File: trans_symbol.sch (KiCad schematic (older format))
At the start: 17 parts, among them J4 Conn_01x04, SW1 SW_SPST, U1 ATSAMD21G18A-AU, U2 MIC5504-3.3YM5, Y1 32768Hz

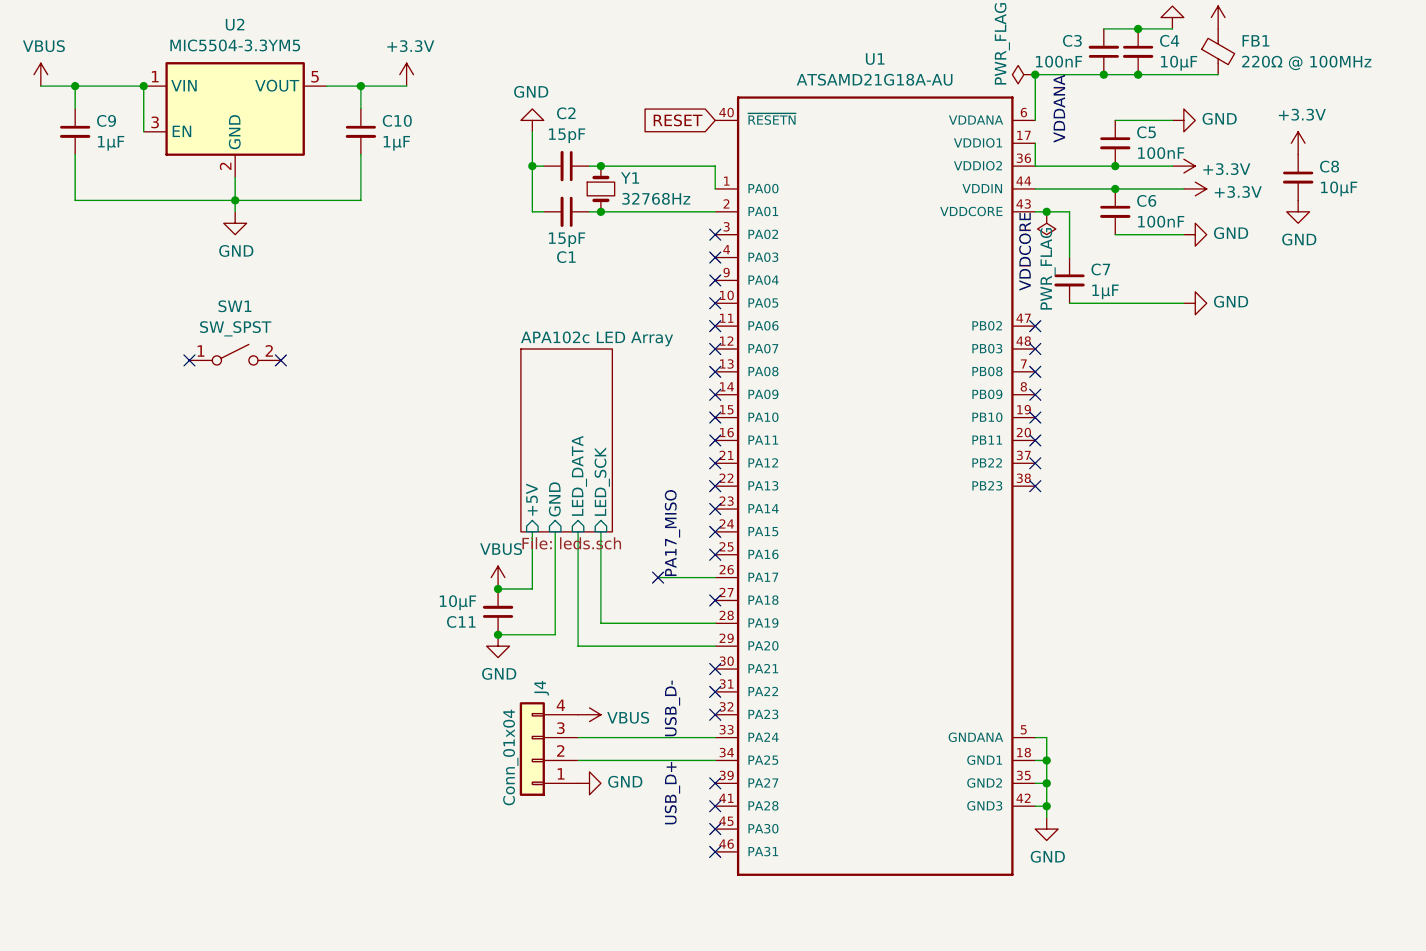
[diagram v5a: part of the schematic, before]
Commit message: add an i2s microphone on default arduino zero i2s pins
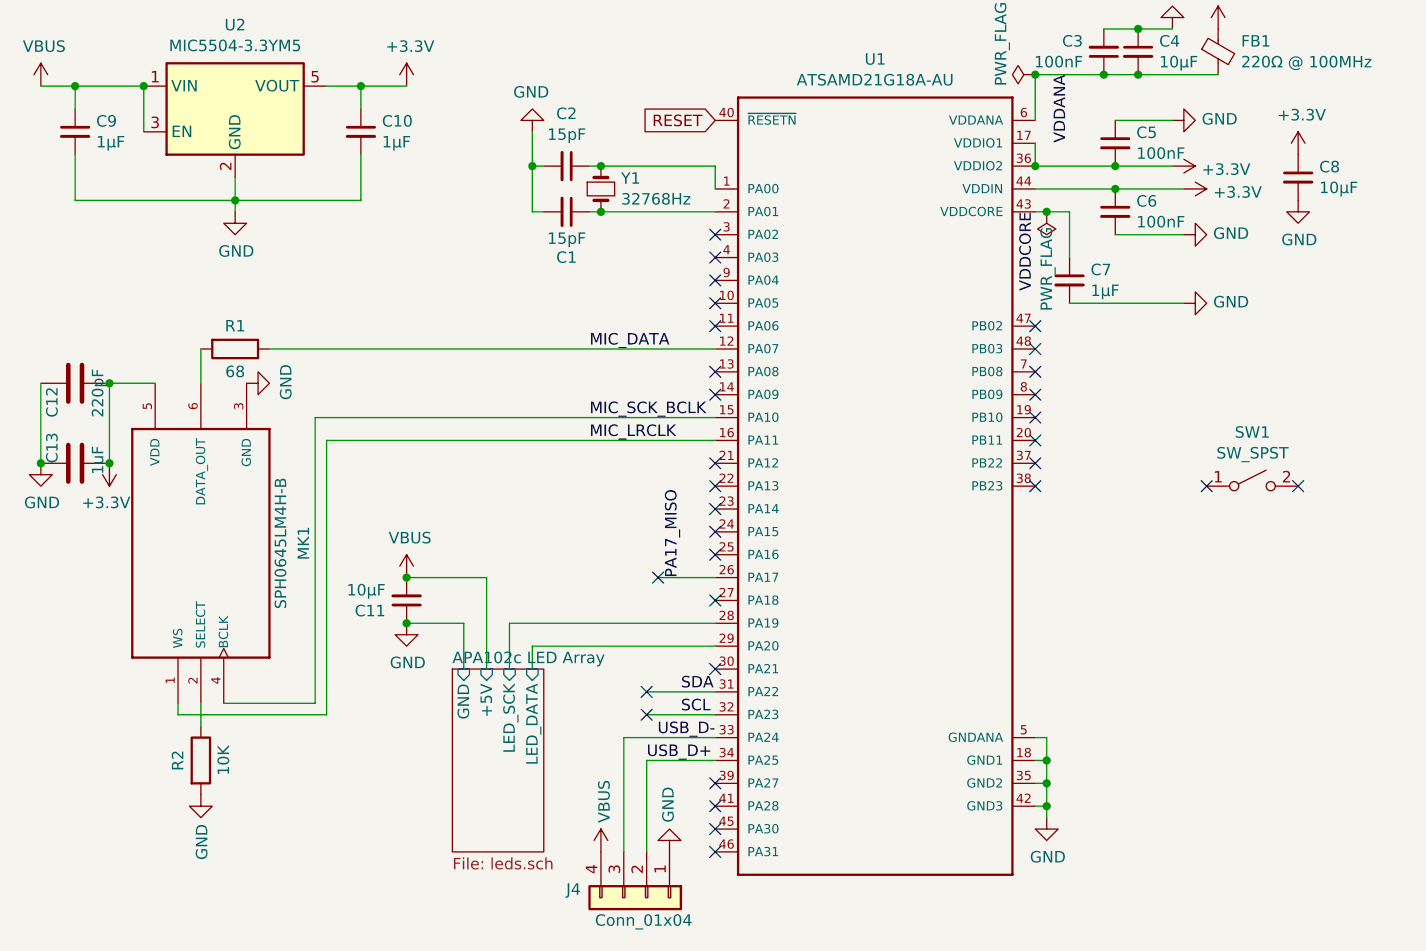
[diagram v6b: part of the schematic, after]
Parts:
- added C12: 220pF, Capacitor_SMD:C_0805_2012Metric, symbol Device:C
- added C13: 1uF, Capacitor_SMD:C_0805_2012Metric, symbol Device:C
- added MK1: SPH0645LM4H-B, Mic-SPH0645LM4H-B:MIC_SPH0645LM4H-B, symbol Mic_I2S_SPH0645LM4H-B:SPH0645LM4H-B
- added R1: 68, Resistor_SMD:R_0805_2012Metric, symbol Device:R
- added R2: 10K, Resistor_SMD:R_0603_1608Metric, symbol Device:R
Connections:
- net +3V3: now also C12.2, C13.2, MK1.5 (VDD)
- net GND: now also C12.1, C13.1, MK1.3 (GND), R2.2
- net MIC_DATA: now reaches U1.12 (PA07)
- net MIC_DATA: now also R1.1
- net MIC_SCK_BCLK: now reaches U1.15 (PA10)
- net MIC_SCK_BCLK: now also MK1.4 (BCLK)
- net MIC_LRCLK: now reaches U1.16 (PA11)
- net MIC_LRCLK: now also MK1.1 (WS)
- net SDA: now reaches U1.31 (PA22)
- net SCL: now reaches U1.32 (PA23)
- new net: MK1.2 (SELECT), R2.1
- new net: MK1.6 (DATA_OUT), R1.2
- no-connect marks 34 -> 31
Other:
- moved on the sheet: C11, J4, SW1

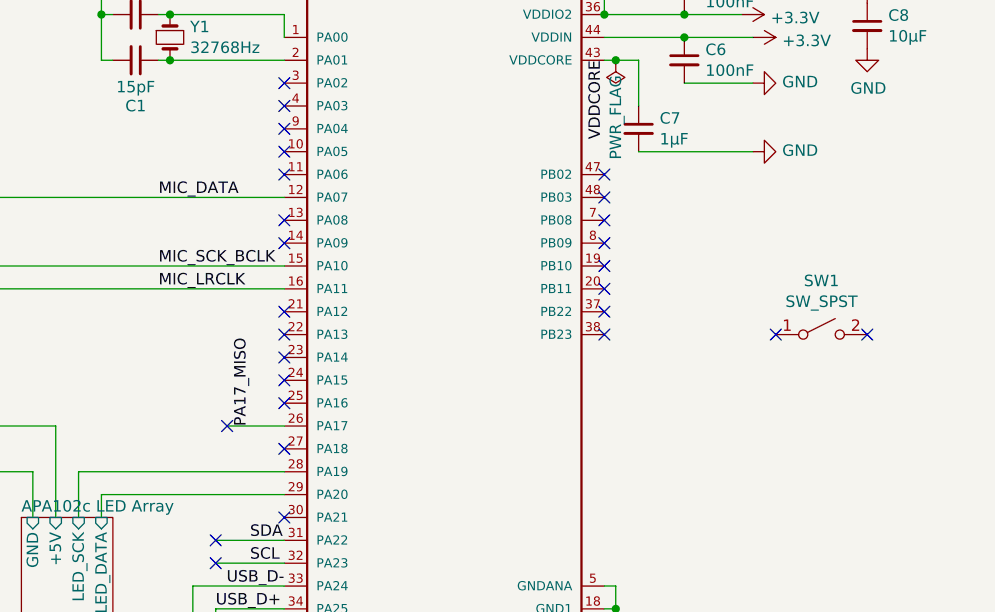
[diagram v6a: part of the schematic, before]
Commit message: add three buttons; untested beacuse I've bricked my samd board again, trying to get it to come back alive
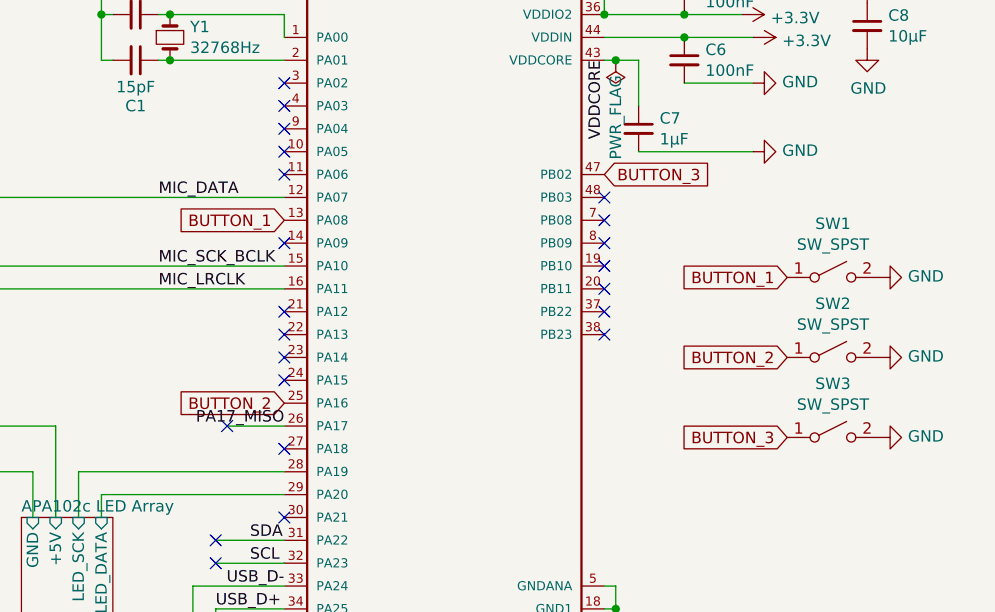
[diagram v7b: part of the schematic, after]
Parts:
- added SW2, SW3: SW_SPST, Button_Switch_SMD:KMR731NG LFS (opal), symbol Switch:SW_SPST
- SW1: footprint Button_Switch_THT:SW_PUSH_6mm_H5mm -> Button_Switch_SMD:KMR731NG LFS (opal)
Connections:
- net GND: now also SW1.2 (B), SW2.2 (B), SW3.2 (B)
- net BUTTON_1: now reaches U1.13 (PA08)
- net BUTTON_1: now also SW1.1 (A)
- net BUTTON_2: now reaches U1.25 (PA16)
- net BUTTON_2: now also SW2.1 (A)
- net BUTTON_3: now reaches U1.47 (PB02)
- net BUTTON_3: now also SW3.1 (A)
- no-connect marks 31 -> 26
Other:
- moved on the sheet: SW1
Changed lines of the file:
@@
 Text Label 3950 4050 2    50   ~ 0
 USB_D-
-NoConn ~ 3950 3250
 NoConn ~ 3950 3150
 NoConn ~ 3950 3050
@@
 NoConn ~ 3950 2850
 NoConn ~ 3950 2550
-NoConn ~ 3950 2450
 NoConn ~ 3950 2250
 NoConn ~ 3950 2150
@@
 NoConn ~ 3950 1950
 NoConn ~ 3950 1850
-NoConn ~ 5350 2250
 NoConn ~ 5350 2350
 NoConn ~ 5350 2450
@@
 	3950 3350 3700 3350
 NoConn ~ 3700 3350
-Text Label 3800 3350 1    50   ~ 0
+Text Label 3950 3350 2    50   ~ 0
 PA17_MISO
 $Comp
@@
 L Switch:SW_SPST SW1
 U 1 1 5FC0D3F5
-P 6300 2950
-F 0 "SW1" H 6300 3185 50  0000 C CNN
-F 1 "SW_SPST" H 6300 3094 50  0000 C CNN
-F 2 "Button_Switch_THT:SW_PUSH_6mm_H5mm" H 6300 2950 50  0001 C CNN
-F 3 "~" H 6300 2950 50  0001 C CNN
-	1    6300 2950
-	1    0    0    -1
-$EndComp
-NoConn ~ 6500 2950
-NoConn ~ 6100 2950
+P 6350 2700
+F 0 "SW1" H 6350 2935 50  0000 C CNN
+F 1 "SW_SPST" H 6350 2844 50  0000 C CNN
+F 2 "Button_Switch_SMD:KMR731NG LFS (opal)" H 6350 2700 50  0001 C CNN
+F 3 "~" H 6350 2700 50  0001 C CNN
+	1    6350 2700
+	1    0    0    -1
+$EndComp
 $Comp
 L ATSAMD21G18A-AU:ATSAMD21G18A-AU U1
@@
 	2250 2750 2250 3950
 $Comp
-L power:+3.3V #PWR?
+L power:+3.3V #PWR0132
 U 1 1 5F97EEE1
 P 1300 2850
-F 0 "#PWR?" H 1300 2700 50  0001 C CNN
+F 0 "#PWR0132" H 1300 2700 50  0001 C CNN
 F 1 "+3.3V" H 1315 3023 50  0000 C CNN
 F 2 "" H 1300 2850 50  0001 C CNN
@@
 $EndComp
 Connection ~ 1300 2850
+$Comp
+L Switch:SW_SPST SW2
+U 1 1 5F9106F9
+P 6350 3050
+F 0 "SW2" H 6350 3285 50  0000 C CNN
+F 1 "SW_SPST" H 6350 3194 50  0000 C CNN
+F 2 "Button_Switch_SMD:KMR731NG LFS (opal)" H 6350 3050 50  0001 C CNN
+F 3 "~" H 6350 3050 50  0001 C CNN
+	1    6350 3050
+	1    0    0    -1
+$EndComp
+$Comp
+L Switch:SW_SPST SW3
+U 1 1 5F910AB5
+P 6350 3400
+F 0 "SW3" H 6350 3635 50  0000 C CNN
+F 1 "SW_SPST" H 6350 3544 50  0000 C CNN
+F 2 "Button_Switch_SMD:KMR731NG LFS (opal)" H 6350 3400 50  0001 C CNN
+F 3 "~" H 6350 3400 50  0001 C CNN
+	1    6350 3400
+	1    0    0    -1
+$EndComp
+$Comp
+L power:GND #PWR?
+U 1 1 5F9110A0
+P 6550 2700
+F 0 "#PWR?" H 6550 2450 50  0001 C CNN
+F 1 "GND" V 6555 2572 50  0000 R CNN
+F 2 "" H 6550 2700 50  0001 C CNN
+F 3 "" H 6550 2700 50  0001 C CNN
+	1    6550 2700
+	0    -1   -1   0
+$EndComp
+$Comp
+L power:GND #PWR?
+U 1 1 5F911146
+P 6550 3050
+F 0 "#PWR?" H 6550 2800 50  0001 C CNN
+F 1 "GND" V 6555 2922 50  0000 R CNN
+F 2 "" H 6550 3050 50  0001 C CNN
+F 3 "" H 6550 3050 50  0001 C CNN
+	1    6550 3050
+	0    -1   -1   0
+$EndComp
+$Comp
+L power:GND #PWR?
+U 1 1 5F9113D1
+P 6550 3400
+F 0 "#PWR?" H 6550 3150 50  0001 C CNN
+F 1 "GND" V 6555 3272 50  0000 R CNN
+F 2 "" H 6550 3400 50  0001 C CNN
+F 3 "" H 6550 3400 50  0001 C CNN
+	1    6550 3400
+	0    -1   -1   0
+$EndComp
+Text GLabel 3950 2450 0    50   Input ~ 0
+BUTTON_1
+Text GLabel 3950 3250 0    50   Input ~ 0
+BUTTON_2
+Text GLabel 5350 2250 2    50   Input ~ 0
+BUTTON_3
+Text GLabel 6150 3400 0    50   Input ~ 0
+BUTTON_3
+Text GLabel 6150 3050 0    50   Input ~ 0
+BUTTON_2
+Text GLabel 6150 2700 0    50   Input ~ 0
+BUTTON_1
 $EndSCHEMATC
